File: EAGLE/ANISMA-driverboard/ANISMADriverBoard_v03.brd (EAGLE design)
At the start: 36.2 x 24 mm, 23 parts

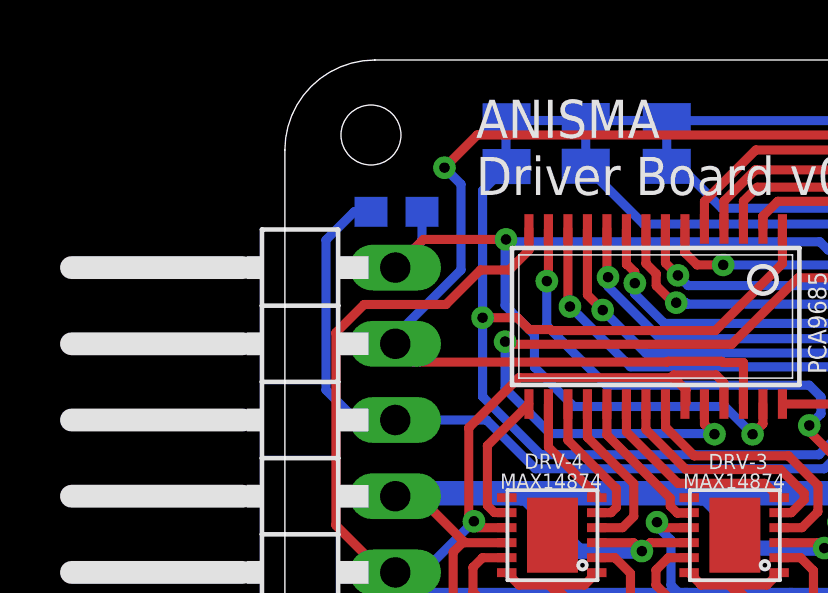
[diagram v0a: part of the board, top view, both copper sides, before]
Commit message: added cam and gerber files
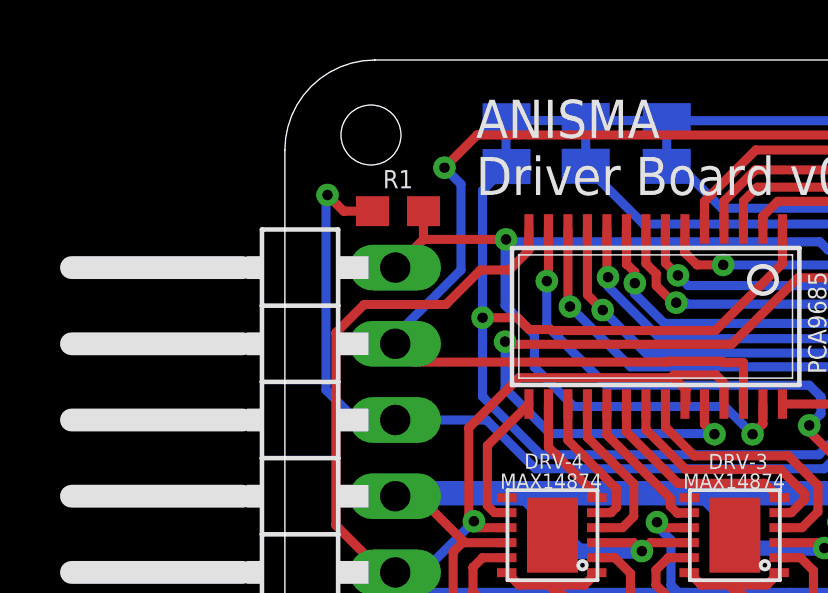
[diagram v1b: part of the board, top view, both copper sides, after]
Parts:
- moved R1 0.05 mm to (5.90, 22.5), flipped to the top, turned to 0 degrees
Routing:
- net VS-5V: track 47.0 -> 48.3 mm, vias 1 -> 2
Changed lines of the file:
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@@
 <layer number="14" name="Route14" color="22" fill="1" visible="no" active="no"/>
 <layer number="15" name="Route15" color="23" fill="1" visible="no" active="no"/>
-<layer number="16" name="Bottom" color="1" fill="1" visible="yes" active="yes"/>
+<layer number="16" name="Bottom" color="1" fill="1" visible="no" active="yes"/>
 <layer number="17" name="Pads" color="2" fill="1" visible="yes" active="yes"/>
 <layer number="18" name="Vias" color="2" fill="1" visible="yes" active="yes"/>
@@
 <layer number="20" name="Dimension" color="24" fill="1" visible="yes" active="yes"/>
 <layer number="21" name="tPlace" color="7" fill="1" visible="yes" active="yes"/>
-<layer number="22" name="bPlace" color="7" fill="1" visible="yes" active="yes"/>
+<layer number="22" name="bPlace" color="7" fill="1" visible="no" active="yes"/>
 <layer number="23" name="tOrigins" color="15" fill="1" visible="yes" active="yes"/>
-<layer number="24" name="bOrigins" color="15" fill="1" visible="yes" active="yes"/>
+<layer number="24" name="bOrigins" color="15" fill="1" visible="no" active="yes"/>
 <layer number="25" name="tNames" color="7" fill="1" visible="yes" active="yes"/>
-<layer number="26" name="bNames" color="7" fill="1" visible="yes" active="yes"/>
+<layer number="26" name="bNames" color="7" fill="1" visible="no" active="yes"/>
 <layer number="27" name="tValues" color="7" fill="1" visible="no" active="yes"/>
 <layer number="28" name="bValues" color="7" fill="1" visible="no" active="yes"/>
@@
 <layer number="38" name="bTest" color="7" fill="1" visible="no" active="yes"/>
 <layer number="39" name="tKeepout" color="4" fill="11" visible="yes" active="yes"/>
-<layer number="40" name="bKeepout" color="1" fill="11" visible="yes" active="yes"/>
+<layer number="40" name="bKeepout" color="1" fill="11" visible="no" active="yes"/>
 <layer number="41" name="tRestrict" color="4" fill="10" visible="yes" active="yes"/>
-<layer number="42" name="bRestrict" color="1" fill="10" visible="yes" active="yes"/>
+<layer number="42" name="bRestrict" color="1" fill="10" visible="no" active="yes"/>
 <layer number="43" name="vRestrict" color="2" fill="10" visible="no" active="yes"/>
 <layer number="44" name="Drills" color="7" fill="1" visible="no" active="yes"/>
@@
 <layer number="50" name="dxf" color="7" fill="1" visible="no" active="no"/>
 <layer number="51" name="tDocu" color="7" fill="1" visible="yes" active="yes"/>
-<layer number="52" name="bDocu" color="7" fill="1" visible="yes" active="yes"/>
+<layer number="52" name="bDocu" color="7" fill="1" visible="no" active="yes"/>
 <layer number="53" name="tGND_GNDA" color="7" fill="9" visible="no" active="no"/>
 <layer number="54" name="bGND_GNDA" color="1" fill="9" visible="no" active="no"/>
@@
 <attribute name="VALUE" x="34.69" y="7.245" size="1.27" layer="27"/>
 </element>
-<element name="R1" library="SparkFun-Resistors" package="0603" value="10k" x="5.85" y="22.44" smashed="yes" rot="MR180">
-<attribute name="NAME" x="5.85" y="21.678" size="0.6096" layer="26" font="vector" ratio="20" rot="MR180" align="bottom-center"/>
-<attribute name="PROD_ID" value="RES-00824" x="5.85" y="22.44" size="1.778" layer="28" rot="MR180" display="off"/>
-<attribute name="SPICEPREFIX" value="R" x="5.85" y="22.44" size="1.778" layer="28" rot="MR180" display="off"/>
-<attribute name="VALUE" x="5.85" y="23.202" size="0.6096" layer="28" font="vector" ratio="20" rot="MR180" align="top-center"/>
+<element name="R1" library="SparkFun-Resistors" package="0603" value="10k" x="5.9" y="22.46" smashed="yes">
+<attribute name="NAME" x="5.9" y="23.222" size="0.6096" layer="25" font="vector" ratio="20" align="bottom-center"/>
+<attribute name="PROD_ID" value="RES-00824" x="5.9" y="22.46" size="1.778" layer="27" display="off"/>
+<attribute name="SPICEPREFIX" value="R" x="5.9" y="22.46" size="1.778" layer="27" display="off"/>
+<attribute name="VALUE" x="5.9" y="21.698" size="0.6096" layer="27" font="vector" ratio="20" align="top-center"/>
 </element>
 <element name="C1" library="EEE1CA470WR" package="CAP_EEE1CA470WR" value="EEE1CA470WR" x="29.5" y="24" smashed="yes" rot="R180">
@@
 <wire x1="33.52" y1="16.67" x2="34.69" y2="15.5" width="0.3048" layer="1"/>
 <contactref element="R1" pad="1"/>
-<wire x1="5" y1="22.44" x2="4.44" y2="22.44" width="0.3048" layer="16"/>
-<wire x1="4.44" y1="22.44" x2="3.5" y2="21.5" width="0.3048" layer="16"/>
-<wire x1="3.5" y1="21.5" x2="3.5" y2="16.5" width="0.3048" layer="16"/>
+<wire x1="3.55" y1="23" x2="3.5" y2="22.95" width="0.3048" layer="16"/>
+<wire x1="3.5" y1="22.95" x2="3.5" y2="16.5" width="0.3048" layer="16"/>
 <wire x1="3.5" y1="16.5" x2="4.5" y2="15.5" width="0.3048" layer="16"/>
 <wire x1="4.5" y1="15.5" x2="5.81" y2="15.5" width="0.3048" layer="16"/>
+<via x="3.55" y="23" extent="1-16" drill="0.35"/>
+<wire x1="3.55" y1="23" x2="4.09" y2="22.46" width="0.3048" layer="1"/>
+<wire x1="4.09" y1="22.46" x2="5.05" y2="22.46" width="0.3048" layer="1"/>
 </signal>
 <signal name="SDA">
@@
 <via x="9.5" y="21.52" extent="1-16" drill="0.35"/>
 <wire x1="9.5" y1="21.52" x2="6.75" y2="21.52" width="0.3048" layer="1"/>
-<wire x1="6.75" y1="21.52" x2="5.81" y2="20.58" width="0.3048" layer="1"/>
+<wire x1="6.615" y1="21.385" x2="5.81" y2="20.58" width="0.3048" layer="1"/>
 <wire x1="10.45" y1="18.34" x2="9.47" y2="19.32" width="0.3048" layer="16"/>
 <wire x1="9.58" y1="21.44" x2="9.5" y2="21.52" width="0.3048" layer="16"/>
@@
 <wire x1="34.103" y1="21.167" x2="20.2370875" y2="21.167" width="0.3048" layer="16"/>
 <contactref element="R1" pad="2"/>
-<wire x1="6.7" y1="22.44" x2="6.7" y2="21.47" width="0.3048" layer="16"/>
 <wire x1="6.7" y1="21.47" x2="5.81" y2="20.58" width="0.3048" layer="16"/>
+<wire x1="6.75" y1="22.46" x2="6.75" y2="21.52" width="0.3048" layer="1"/>
+<wire x1="6.75" y1="21.52" x2="6.615" y2="21.385" width="0.3048" layer="1"/>
 </signal>
 <signal name="SCL">
